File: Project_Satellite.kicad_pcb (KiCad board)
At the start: 2 copper layers, 64 parts, among them J1 Conn_01x02_Socket, J10 Conn_01x01_Socket, J11 Conn_01x01_Socket, J12 Conn_01x01_Socket, J15 Conn_01x01_Socket, J5 Conn_01x02_Socket, J6 Conn_01x02_Socket, J7 Conn_01x01_Socket, J8 Conn_01x02_Socket, J9 Conn_01x02_Socket, U3 TPS62933, U4 RASPBERRY_PI_ZERO_2_W, U5 TLV320AIC3254IRHBR, U6 MEMSMic, U7 MEMSMic, U8 TPA3118D2DAPR

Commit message: Laying out PCB components
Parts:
- removed C10, C9: 22uF, Capacitor_SMD:C_1206_3216Metric_Pad1.33x1.80mm_HandSolder
- removed C11, C12, C14, C5, C6: 0.1uF, Capacitor_SMD:C_0805_2012Metric_Pad1.18x1.45mm_HandSolder
- removed C13, C27: 1uF, Capacitor_SMD:C_0603_1608Metric_Pad1.08x0.95mm_HandSolder
- removed C34: 33nF, Capacitor_SMD:C_0603_1608Metric_Pad1.08x0.95mm_HandSolder
- removed C7, C8: 10uF, Capacitor_SMD:C_1206_3216Metric_Pad1.33x1.80mm_HandSolder
- removed J1, J5, J6: Conn_01x02_Socket, Connector_PinHeader_2.54mm:PinHeader_1x02_P2.54mm_Horizontal
- removed J15: Conn_01x01_Socket, Connector_PinHeader_2.54mm:PinHeader_1x01_P2.54mm_Horizontal
- removed L1: 6.8 uH, Inductor_SMD:L_APV_APH0630
- removed R1: 10.2k, Resistor_SMD:R_0603_1608Metric_Pad0.98x0.95mm_HandSolder
- removed R2: 53.6k, Resistor_SMD:R_0603_1608Metric_Pad0.98x0.95mm_HandSolder
- removed R3: 50, Resistor_SMD:R_0805_2012Metric_Pad1.20x1.40mm_HandSolder
- removed R6: 5.6k, Resistor_SMD:R_0603_1608Metric_Pad0.98x0.95mm_HandSolder
- removed TP1: TestPoint, Connector_PinHeader_2.54mm:PinHeader_1x01_P2.54mm_Horizontal
- removed U3: TPS62933, Package_TO_SOT_SMD:SOT-583-8
- removed U8: TPA3118D2DAPR, MyFootprints:TPA3118
- added 0.1uF: 0.1uF, Capacitor_SMD:C_0805_2012Metric_Pad1.18x1.45mm_HandSolder, F.Cu at (98.5, 37.5)
- added 0.1uF: 0.1uF, Capacitor_SMD:C_0805_2012Metric_Pad1.18x1.45mm_HandSolder, F.Cu at (89.0, 63.8)
- added 0.1uF: 0.1uF, Capacitor_SMD:C_0805_2012Metric_Pad1.18x1.45mm_HandSolder, F.Cu at (92.5, 42.8)
- added 0.1uF: 0.1uF, Capacitor_SMD:C_0805_2012Metric_Pad1.18x1.45mm_HandSolder, F.Cu at (71.0, 42.8)
- added 0.1uF: 0.1uF, Capacitor_SMD:C_0805_2012Metric_Pad1.18x1.45mm_HandSolder, F.Cu at (75.5, 37.7)
- added 0.1uF: 0.1uF, Capacitor_SMD:C_0805_2012Metric_Pad1.18x1.45mm_HandSolder, F.Cu at (80.5, 42.0)
- added 10.2k: 10.2k, Resistor_SMD:R_0603_1608Metric_Pad0.98x0.95mm_HandSolder, F.Cu at (81.2, 37.5)
- added 10uF: 10uF, Capacitor_SMD:C_1206_3216Metric_Pad1.33x1.80mm_HandSolder, F.Cu at (71.2, 38.2)
- added 10uF: 10uF, Capacitor_SMD:C_1206_3216Metric_Pad1.33x1.80mm_HandSolder, F.Cu at (75.2, 42.3)
- added 1uF: 1uF, Capacitor_SMD:C_0603_1608Metric_Pad1.08x0.95mm_HandSolder, F.Cu at (89.0, 65.5)
- added 1uF: 1uF, Capacitor_SMD:C_0603_1608Metric_Pad1.08x0.95mm_HandSolder, F.Cu at (62.0, 55.2)
- added 22uF: 22uF, Capacitor_SMD:C_1206_3216Metric_Pad1.33x1.80mm_HandSolder, F.Cu at (91.7, 46.3)
- added 22uF: 22uF, Capacitor_SMD:C_1206_3216Metric_Pad1.33x1.80mm_HandSolder, F.Cu at (91.0, 39.2)
- added 33nF: 33nF, Capacitor_SMD:C_0603_1608Metric_Pad1.08x0.95mm_HandSolder, F.Cu at (81.2, 39.2)
- added 5.6k: 5.6k, Resistor_SMD:R_0603_1608Metric_Pad0.98x0.95mm_HandSolder, F.Cu at (62.0, 56.8)
- added 50: 50, Resistor_SMD:R_0805_2012Metric_Pad1.20x1.40mm_HandSolder, F.Cu at (89.2, 35.5)
- added 53.6k: 53.6k, Resistor_SMD:R_0603_1608Metric_Pad0.98x0.95mm_HandSolder, F.Cu at (85.5, 36.0)
- added 6.8uH: 6.8 uH, Inductor_SMD:L_APV_APH0630, F.Cu at (86.0, 43.8)
- added EN: Conn_01x01_Socket, Connector_PinHeader_2.54mm:PinHeader_1x01_P2.54mm_Vertical, F.Cu at (76.0, 46.8)
- added MCLK: TestPoint, Connector_PinHeader_2.54mm:PinHeader_1x01_P2.54mm_Horizontal, F.Cu at (95.5, 66.5)
- added Power In: Conn_01x02_Socket, Connector_PinHeader_2.54mm:PinHeader_1x02_P2.54mm_Vertical, F.Cu at (68.2, 39.0)
- added SDA: Conn_01x02_Socket, Connector_PinHeader_2.54mm:PinHeader_1x02_P2.54mm_Vertical, F.Cu at (94.7, 54.2)
- added SDA: Conn_01x02_Socket, Connector_PinHeader_2.54mm:PinHeader_1x02_P2.54mm_Vertical, F.Cu at (97.8, 45.5)
- added TPA3118: TPA3118D2DAPR, MyFootprints:TPA3118, F.Cu at (68.5, 56.8)
- added TPS62933: TPS62933, Package_TO_SOT_SMD:SOT-583-8, F.Cu at (78.0, 38.5)
- J10, J11, J12, J7: footprint Connector_PinHeader_2.54mm:PinHeader_1x01_P2.54mm_Horizontal -> Connector_PinHeader_2.54mm:PinHeader_1x01_P2.54mm_Vertical
- J8, J9: footprint Connector_PinHeader_2.54mm:PinHeader_1x02_P2.54mm_Horizontal -> Connector_PinHeader_2.54mm:PinHeader_1x02_P2.54mm_Vertical
- moved R7 213.9 mm to (52.5, 73.2)
- moved J10 202.3 mm to (46.0, 46.2)
- moved J12 198.1 mm to (53.2, 78.0)
- moved C22 190.1 mm to (62.0, 53.5)
- moved U5 171.6 mm to (92.0, 59.5), turned to 180 degrees
- moved R4 158.0 mm to (109.5, 37.0)
- moved U4 116.2 mm to (101.5, 36.3)
- moved D1 111.6 mm to (113.5, 38.2)
- moved C15 70.1 mm to (183.3, 56.5)
- moved C23 70.1 mm to (183.3, 59.5)
- moved C26 70.1 mm to (183.3, 62.5)
- moved C28 70.1 mm to (183.3, 65.5)
- moved C36 70.1 mm to (188.1, 56.5)
- moved C37 70.1 mm to (188.1, 59.5)
- moved C38 70.1 mm to (188.1, 62.5)
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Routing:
- net +15V: track 0.00 -> 1.76 mm, vias 0 -> 4
- net GND: track 0.00 -> 0.25 mm, vias 0 -> 10
- net +5V: vias 0 -> 8
- added copper zone on B.Cu, net GND
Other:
- copper layers 2 -> 4
- board text added: "SCL"

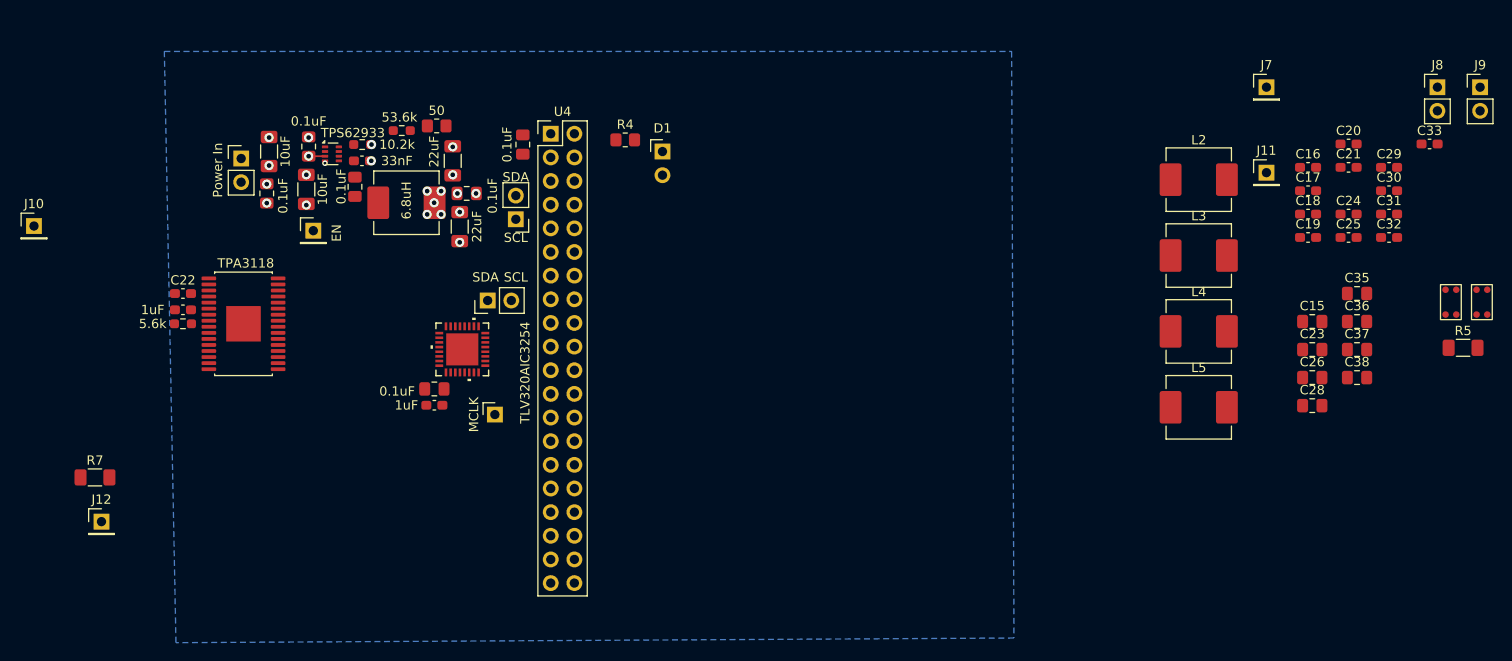
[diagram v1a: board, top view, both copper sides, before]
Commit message: Initial placement and routing done. Need to fix DRC errors/warnings and create mic cutoff areas
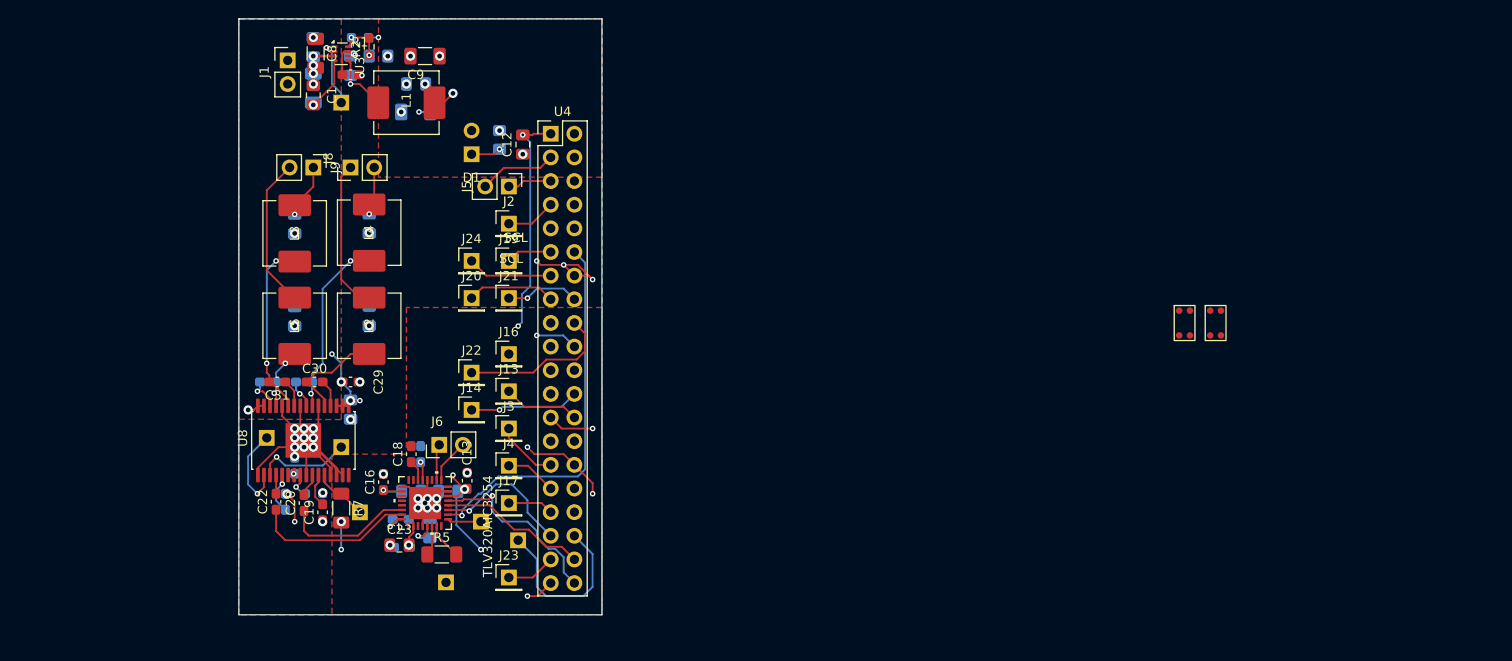
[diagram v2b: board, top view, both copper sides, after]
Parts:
- added J13: Conn_01x01_Socket, Connector_PinHeader_2.54mm:PinHeader_1x01_P2.54mm_Vertical, F.Cu at (97.0, 64.0)
- added J14: Conn_01x01_Socket, Connector_PinHeader_2.54mm:PinHeader_1x01_P2.54mm_Vertical, F.Cu at (93.0, 66.0)
- added J16: Conn_01x01_Socket, Connector_PinHeader_2.54mm:PinHeader_1x01_P2.54mm_Vertical, F.Cu at (97.0, 60.0)
- added J17: Conn_01x01_Socket, Connector_PinHeader_2.54mm:PinHeader_1x01_P2.54mm_Vertical, F.Cu at (97.0, 76.0)
- added J18: Conn_01x01_Socket, Connector_PinHeader_2.54mm:PinHeader_1x01_P2.54mm_Vertical, B.Cu at (98.0, 80.0)
- added J19: Conn_01x01_Socket, Connector_PinHeader_2.54mm:PinHeader_1x01_P2.54mm_Vertical, F.Cu at (97.0, 50.0)
- added J2: Conn_01x01_Socket, Connector_PinHeader_2.54mm:PinHeader_1x01_P2.54mm_Vertical, F.Cu at (97.0, 46.0)
- added J20: Conn_01x01_Socket, Connector_PinHeader_2.54mm:PinHeader_1x01_P2.54mm_Vertical, F.Cu at (93.0, 54.0)
- added J21: Conn_01x01_Socket, Connector_PinHeader_2.54mm:PinHeader_1x01_P2.54mm_Vertical, F.Cu at (97.0, 54.0)
- added J22: Conn_01x01_Socket, Connector_PinHeader_2.54mm:PinHeader_1x01_P2.54mm_Vertical, F.Cu at (93.0, 62.0)
- added J23: Conn_01x01_Socket, Connector_PinHeader_2.54mm:PinHeader_1x01_P2.54mm_Vertical, F.Cu at (97.0, 84.0)
- added J24: Conn_01x01_Socket, Connector_PinHeader_2.54mm:PinHeader_1x01_P2.54mm_Vertical, F.Cu at (93.0, 50.0)
- added J3: Conn_01x01_Socket, Connector_PinHeader_2.54mm:PinHeader_1x01_P2.54mm_Vertical, F.Cu at (97.0, 68.0)
- added J4: Conn_01x01_Socket, Connector_PinHeader_2.54mm:PinHeader_1x01_P2.54mm_Vertical, F.Cu at (97.0, 72.0)
- C10: renamed from 22uF; moved to B.Cu
- C11, C14, C5, C6: renamed from 0.1uF; moved to B.Cu
- C15, C17, C21, C24, C25, C26, C28, C32, C33, C35, C36, C37, C38, D1, J10, J11, J12, J7, R4: moved to B.Cu
- C27: renamed from 1uF; moved to B.Cu
- C7: renamed from 10uF; moved to B.Cu
- J1: renamed from Power In
- J15: renamed from EN; moved to B.Cu
- R1: renamed from 10.2k; moved to B.Cu
- R3: renamed from 50; moved to B.Cu
- R6: renamed from 5.6k; moved to B.Cu
- TP1: renamed from MCLK; moved to B.Cu
- moved C33 127.3 mm to (71.1, 63.0)
- moved J9 125.6 mm to (76.0, 40.0), turned to -90 degrees
- moved C31 120.8 mm to (72.1, 63.0), turned to 180 degrees
- moved C21 119.7 mm to (73.0, 75.9), turned to -90 degrees
- moved C20 118.6 mm to (75.0, 76.0), turned to 90 degrees
- moved C32 117.6 mm to (75.0, 63.0)
- moved C30 117.2 mm to (76.1, 63.0)
- moved J8 117.0 mm to (80.0, 40.0), turned to 90 degrees
- moved C36 114.6 mm to (74.0, 46.0), turned to 90 degrees
- moved C38 114.3 mm to (74.0, 56.0), turned to -90 degrees
- moved C29 113.9 mm to (80.0, 63.0), turned to 180 degrees
- moved R5 111.9 mm to (89.8, 81.5)
- moved C19 109.9 mm to (77.0, 77.0), turned to 90 degrees
- moved C24 107.8 mm to (85.5, 80.8)
- moved C37 107.0 mm to (82.0, 46.0), turned to -90 degrees
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- renumbered 0.1uF to C1, 0.1uF to C12, 1uF to C13, 33nF to C34, 10uF to C8, 22uF to C9, SDA to J5, SDA to J6, 6.8uH to L1, 53.6k to R2, TPS62933 to U3, TPA3118 to U8
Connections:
- C36 pad 2: Net-(J8-Pin_2) -> Net-(J9-Pin_1)
- C37 pad 1: Net-(J9-Pin_1) -> Net-(J8-Pin_2)
- J12 pad 1: +3.3V -> Net-(J12-Pin_1)
- L3 pad 2: Net-(J8-Pin_2) -> Net-(J9-Pin_1)
- L4 pad 2: Net-(J9-Pin_1) -> Net-(J8-Pin_2)
- R7 pad 1: Net-(U8-MUTE) -> Net-(J12-Pin_1)
- U4 pad 11: unconnected-(U4-GPIO17/GPIO_GEN0-Pad11) -> Net-(J19-Pin_1)
- U4 pad 13: unconnected-(U4-GPIO27/GPIO_GEN2-Pad13) -> Net-(J24-Pin_1)
- U4 pad 15: unconnected-(U4-GPIO22/GPIO_GEN3-Pad15) -> Net-(J20-Pin_1)
- U4 pad 16: unconnected-(U4-GPIO23/GPIO_GEN4-Pad16) -> Net-(J21-Pin_1)
- U4 pad 18: unconnected-(U4-GPIO24/GPIO_GEN5-Pad18) -> Net-(J22-Pin_1)
- U4 pad 24: unconnected-(U4-GPIO8/SPI_~{CE0}-Pad24) -> Net-(J14-Pin_1)
- U4 pad 26: unconnected-(U4-GPIO7/SPI_~{CE1}-Pad26) -> Net-(J13-Pin_1)
- U4 pad 29: unconnected-(U4-GPIO5-Pad29) -> Net-(J3-Pin_1)
- U4 pad 31: unconnected-(U4-GPIO6-Pad31) -> Net-(J4-Pin_1)
- U4 pad 32: unconnected-(U4-GPIO12-Pad32) -> Net-(J16-Pin_1)
- U4 pad 33: unconnected-(U4-GPIO13-Pad33) -> Net-(J17-Pin_1)
- U4 pad 36: unconnected-(U4-GPIO16-Pad36) -> Net-(J18-Pin_1)
- U4 pad 37: unconnected-(U4-GPIO26-Pad37) -> Net-(J23-Pin_1)
- U4 pad 7: unconnected-(U4-GPIO4/GPIO_GCLK-Pad7) -> Net-(J2-Pin_1)
- U8 pad 12: Net-(U8-MUTE) -> Net-(J12-Pin_1)
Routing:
- net GND: track 0.25 -> 93.3 mm, vias 10 -> 46
- net +3.3V: track 0.00 -> 46.3 mm, vias 0 -> 8
- net Net-(U4-GPIO18/GPIO_GEN1): track 0.00 -> 41.0 mm, vias 0 -> 1
- net Net-(U4-GPIO21): track 0.00 -> 20.0 mm, vias 0 -> 1
- net Net-(U8-OUTPL): track 0.00 -> 19.4 mm, vias 0 -> 2
- net Net-(U8-OUTNR): track 0.00 -> 19.1 mm, vias 0 -> 2
- net Net-(J18-Pin_1): track 0.00 -> 18.9 mm
- net Net-(U5-LOR): track 0.00 -> 17.4 mm
- net Net-(J22-Pin_1): track 0.00 -> 16.6 mm
- net Net-(J9-Pin_2): track 0.00 -> 16.3 mm
- net Net-(J8-Pin_1): track 0.00 -> 16.3 mm
- net Net-(U4-GPIO20): track 0.00 -> 16.0 mm
- net Net-(U4-GPIO19): track 0.00 -> 15.3 mm, vias 0 -> 1
- net +15V: track 1.76 -> 16.9 mm, vias 4 -> 9
- net Net-(U5-LOL): track 0.00 -> 14.0 mm
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- added copper zone on F.Cu, net +15V
- added copper zone on F.Cu, net +3.3V
- added copper zone on F.Cu, net +5V
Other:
- board outline added: 39 x 64 mm

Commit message: Finished PCB design, do quick check and fabricate
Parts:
- added J25: Conn_01x03_Socket, Connector_PinHeader_2.54mm:PinHeader_1x03_P2.54mm_Vertical, F.Cu at (71.4, 82.2)
- added J26: Conn_01x03_Socket, Connector_PinHeader_2.54mm:PinHeader_1x03_P2.54mm_Vertical, F.Cu at (80.7, 84.8)
- added J27: Conn_01x03_Socket, Connector_PinHeader_2.54mm:PinHeader_1x03_P2.54mm_Vertical, F.Cu at (95.5, 29.8)
- added J28: Conn_01x03_Socket, Connector_PinHeader_2.54mm:PinHeader_1x03_P2.54mm_Vertical, F.Cu at (95.7, 25.0)
- J18, J7, TP1: moved to F.Cu
- moved U7 73.8 mm to (106.4, 27.6)
- moved U6 68.9 mm to (106.1, 32.6)
- moved J10 16.6 mm to (87.0, 64.5)
- moved J11 4.37 mm to (83.0, 68.2)
- moved TP1 1.52 mm to (94.2, 79.5), turned to 0 degrees
- moved J18 0.25 mm to (97.8, 80.0), turned to 0 degrees
- turned J7 to 0 degrees
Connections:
- C12 pad 2: +3.3V -> +3V3
- C17 pad 1: Net-(U6-Out) -> Net-(J25-Pin_2)
- C18 pad 2: Net-(U7-Out) -> Net-(J26-Pin_2)
- U4 pad 1: +3.3V -> +3V3
- U6 pad 1: Net-(U6-Out) -> Net-(J27-Pin_2)
- U6 pad 2: /MICBIAS -> Net-(J27-Pin_1)
- U6 pad 3: GND -> Net-(J27-Pin_3)
- U6 pad 4: GND -> Net-(J27-Pin_3)
- U7 pad 1: Net-(U7-Out) -> Net-(J28-Pin_2)
- U7 pad 2: /MICBIAS -> Net-(J28-Pin_1)
- U7 pad 3: GND -> Net-(J28-Pin_3)
- U7 pad 4: GND -> Net-(J28-Pin_3)
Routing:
- net /MICBIAS: track 0.00 -> 25.2 mm, vias 0 -> 2
- net Net-(J16-Pin_1): track 0.00 -> 24.3 mm, vias 0 -> 1
- net Net-(J25-Pin_2): track 0.00 -> 21.8 mm
- net Net-(J10-Pin_1): track 9.53 -> 28.8 mm, vias 1 -> 2
- net Net-(J26-Pin_2): track 0.00 -> 17.5 mm, vias 0 -> 1
- net +3.3V: track 46.3 -> 33.6 mm, vias 8 -> 6
- net Net-(J28-Pin_2): track 0.00 -> 10.9 mm
- net Net-(J28-Pin_1): track 0.00 -> 10.9 mm, vias 0 -> 2
- net Net-(J27-Pin_1): track 0.00 -> 10.6 mm, vias 0 -> 2
- net Net-(J27-Pin_2): track 0.00 -> 10.4 mm
- net Net-(J27-Pin_3): track 0.00 -> 6.72 mm
- net Net-(J28-Pin_3): track 0.00 -> 6.62 mm
- net Net-(J11-Pin_1): track 10.4 -> 15.1 mm
- net Net-(J7-Pin_1): track 3.92 -> 7.38 mm
- net +3V3: track 0.00 -> 3.05 mm
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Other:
- board size 39 x 64 mm -> 40.2 x 65.5 mm
- board text added: "Project Symphony Anjan Godavarti V1"
- board text removed: "SCL"

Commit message: Finished board V1
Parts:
- C30, C31: moved to B.Cu
- C33: moved to F.Cu
- moved C30 4.96 mm to (81.0, 62.0)
- moved C29 3.86 mm to (83.7, 64.0)
- moved C32 2.24 mm to (77.0, 62.0)
- moved C33 1.41 mm to (70.1, 62.0)
- moved C31 1.32 mm to (73.0, 62.0)
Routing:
- net +15V: track 16.2 -> 62.1 mm, vias 9 -> 11
- net Net-(U8-BSNL): track 2.91 -> 6.21 mm, vias 0 -> 1
- net Net-(U8-OUTNL): track 11.4 -> 8.23 mm, vias 0 -> 2
- net GND: track 94.5 -> 91.9 mm, vias 37 -> 38
- net Net-(U8-OUTNR): track 19.1 -> 16.8 mm
- net Net-(U8-OUTPR): track 6.57 -> 8.39 mm, vias 2 -> 0
- net Net-(U8-BSPR): track 3.57 -> 4.42 mm, vias 1 -> 0
- net Net-(U8-BSPL): track 3.09 -> 3.93 mm
- net Net-(U8-BSNR): track 2.95 -> 3.60 mm, vias 0 -> 1
- net Net-(U8-OUTPL): track 19.4 -> 19.3 mm, vias 2 -> 3

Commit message: Final V1 commit
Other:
- copper layers 4 -> 2
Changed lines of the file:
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@@
 	(layers
 		(0 "F.Cu" signal)
-		(4 "In1.Cu" power "PWR.Cu")
-		(6 "In2.Cu" power "GND.Cu")
 		(2 "B.Cu" signal)
 		(9 "F.Adhes" user "F.Adhesive")
@@
 			)
 			(layer "dielectric 1"
-				(type "prepreg")
-				(thickness 0.1)
-				(material "FR4")
-				(epsilon_r 4.5)
-				(loss_tangent 0.02)
-			)
-			(layer "In1.Cu"
-				(type "copper")
-				(thickness 0.035)
-			)
-			(layer "dielectric 2"
 				(type "core")
-				(thickness 1.24)
-				(material "FR4")
-				(epsilon_r 4.5)
-				(loss_tangent 0.02)
-			)
-			(layer "In2.Cu"
-				(type "copper")
-				(thickness 0.035)
-			)
-			(layer "dielectric 3"
-				(type "prepreg")
-				(thickness 0.1)
+				(thickness 1.51)
 				(material "FR4")
 				(epsilon_r 4.5)
@@
 			(plot_on_all_layers_selection 0x00000000_00000000_00000000_00000000)
 			(disableapertmacros no)
-			(usegerberextensions no)
+			(usegerberextensions yes)
 			(usegerberattributes yes)
 			(usegerberadvancedattributes yes)
@@
 			(outputformat 1)
 			(mirror no)
-			(drillshape 1)
+			(drillshape 0)
 			(scaleselection 1)
-			(outputdirectory "")
+			(outputdirectory "V1_Fabrication/")
 		)
 	)
